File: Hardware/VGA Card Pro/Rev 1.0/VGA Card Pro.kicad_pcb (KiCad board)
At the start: 2 copper layers, 100 x 57.6 mm, 34 parts, among them J1 6502 Card Edge, J2 INT Select, J3 DE15_Receptacle_HighDensity_M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, J4 Conn_02x08_Odd_Even, Q1 BSS138, U1 Raspberry Pi Pico, U2 74LVC245, U3 74HCT245, U4 74LVC1G04, U5 74LVC245, U6 74HC138, U7 74HC138

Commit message: VGA Card layout
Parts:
- added C3: 100nF, Capacitor_SMD:C_0805_2012Metric, F.Cu at (148.0, 107.9)
- added C4: 100nF, Capacitor_SMD:C_0805_2012Metric, F.Cu at (178.2, 103.5)
- added C5: 100nF, Capacitor_SMD:C_0805_2012Metric, F.Cu at (118.8, 75.0)
- added C6: 100nF, Capacitor_SMD:C_0805_2012Metric, F.Cu at (168.4, 107.9)
- added C7: 100nF, Capacitor_SMD:C_0805_2012Metric, F.Cu at (115.3, 106.8)
- J3: value DE15_Receptacle_HighDensity_MountingHoles -> VGA
- moved R9 60.5 mm to (177.7, 95.6), turned to 0 degrees
- moved R10 56.5 mm to (177.7, 91.8), turned to 0 degrees
- moved R11 56.4 mm to (177.7, 99.5), turned to 0 degrees
- moved JP4 51.8 mm to (127.7, 118.4), turned to -90 degrees
- moved R5 51.6 mm to (171.9, 85.0), turned to 0 degrees
- moved JP3 51.4 mm to (124.8, 118.4)
- moved R6 49.8 mm to (171.9, 91.8), turned to 0 degrees
- moved R12 48.6 mm to (177.7, 81.1), turned to 0 degrees
- moved R7 48.0 mm to (171.9, 95.6), turned to 0 degrees
- moved R8 46.6 mm to (171.9, 99.5), turned to 0 degrees
- moved C1 46.2 mm to (127.7, 106.8), turned to 180 degrees
- moved R3 46.2 mm to (171.9, 77.2), turned to 0 degrees
- moved U2 44.4 mm to (162.9, 110.0), turned to 90 degrees
- moved R4 42.8 mm to (171.9, 81.1), turned to 0 degrees
- moved U4 42.1 mm to (174.2, 103.5), turned to 0 degrees
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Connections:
- C2 pad 1: VCC -> 3V3
- U4 pad 1: (no net) -> unconnected-(U4-NC-Pad1)
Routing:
- net CSB: track 22.4 -> 50.8 mm, vias 1 -> 2
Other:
- board text added: "IRQB"
- board text added: "JLCJLCJLCJLC"
- board text added: "NMIB"

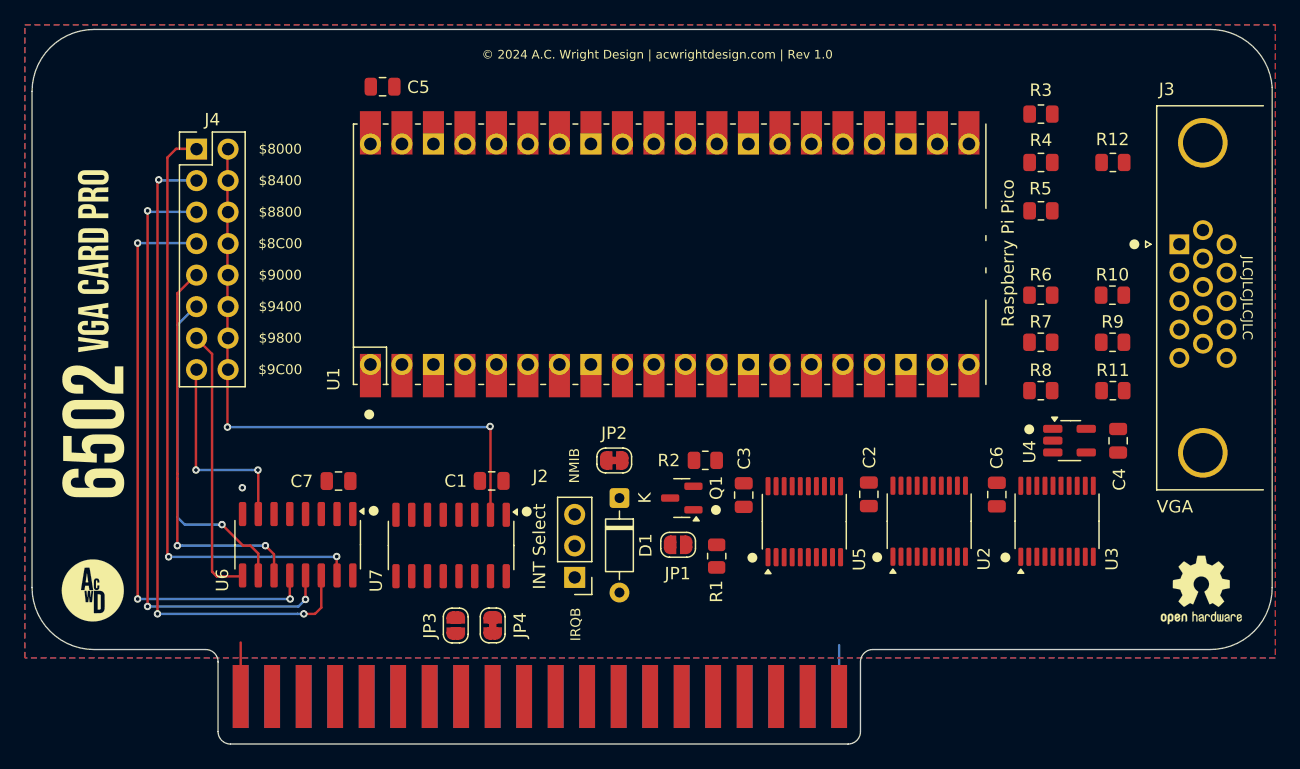
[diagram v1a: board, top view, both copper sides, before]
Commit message: Switch to 74LVC4245s
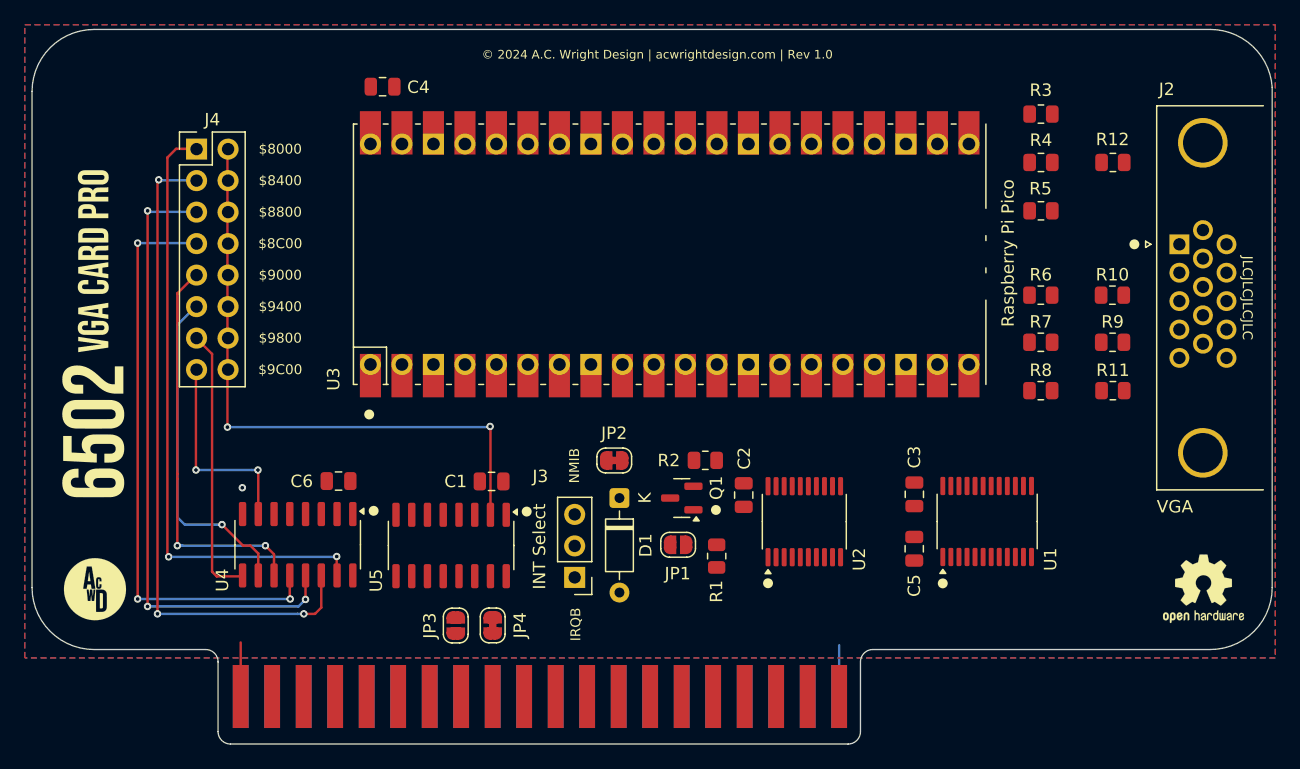
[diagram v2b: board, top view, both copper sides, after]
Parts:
- removed the C1 at (127.7, 106.8)
- removed the U2 at (162.9, 110.0)
- removed the U3 at (173.2, 110.0)
- removed the U4 at (174.2, 103.5)
- added U1: SN74LVC4245APWR, Package_SO:TSSOP-24_4.4x7.8mm_P0.65mm, F.Cu at (167.6, 110.0)
- U5: renamed from U7; value 74HC138 -> 74LVC138
- moved C1 30.4 mm to (127.6, 106.8), turned to 180 degrees
- moved C3 17.0 mm to (161.7, 107.9)
- moved C5 7.97 mm to (161.7, 112.2), turned to 90 degrees
- moved G*** 0.20 mm to (95.7, 115.5)
- moved REF** 0.20 mm to (185.0, 115.5)
- renumbered C2 to C1, C3 to C2, C4 to C3, C5 to C4, C6 to C5, C7 to C6, J3 to J2, J2 to J3, U5 to U2, U1 to U3, U6 to U4
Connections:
- J1 pad A3: unconnected-(J1-PadA3) -> A3
- U2 pad 13: unconnected-(U5-B5-Pad13) -> CSB_3V3
- U2 pad 14: unconnected-(U5-B4-Pad14) -> RESB_3V3
- U2 pad 15: RESB_3V3 -> A3_3V3
- U2 pad 5: RESB -> A3
- U2 pad 6: GND -> RESB
- U2 pad 7: GND -> CSB
- U3 pad 16: CSRB_3V3 -> A2_3V3
- U3 pad 17: CSWB_3V3 -> INTB_3V3
- U3 pad 29: A2_3V3 -> A3_3V3
- U3 pad 31: INTB_3V3 -> RESB_3V3
- U3 pad 32: RESB_3V3 -> CSB_3V3
- U3 pad 34: OEB_3V3 -> RWB_3V3
- U5 pad 14: CSRB_3V3 -> RWBB_3V3
- U5 pad 15: CSWB_3V3 -> RWB_3V3

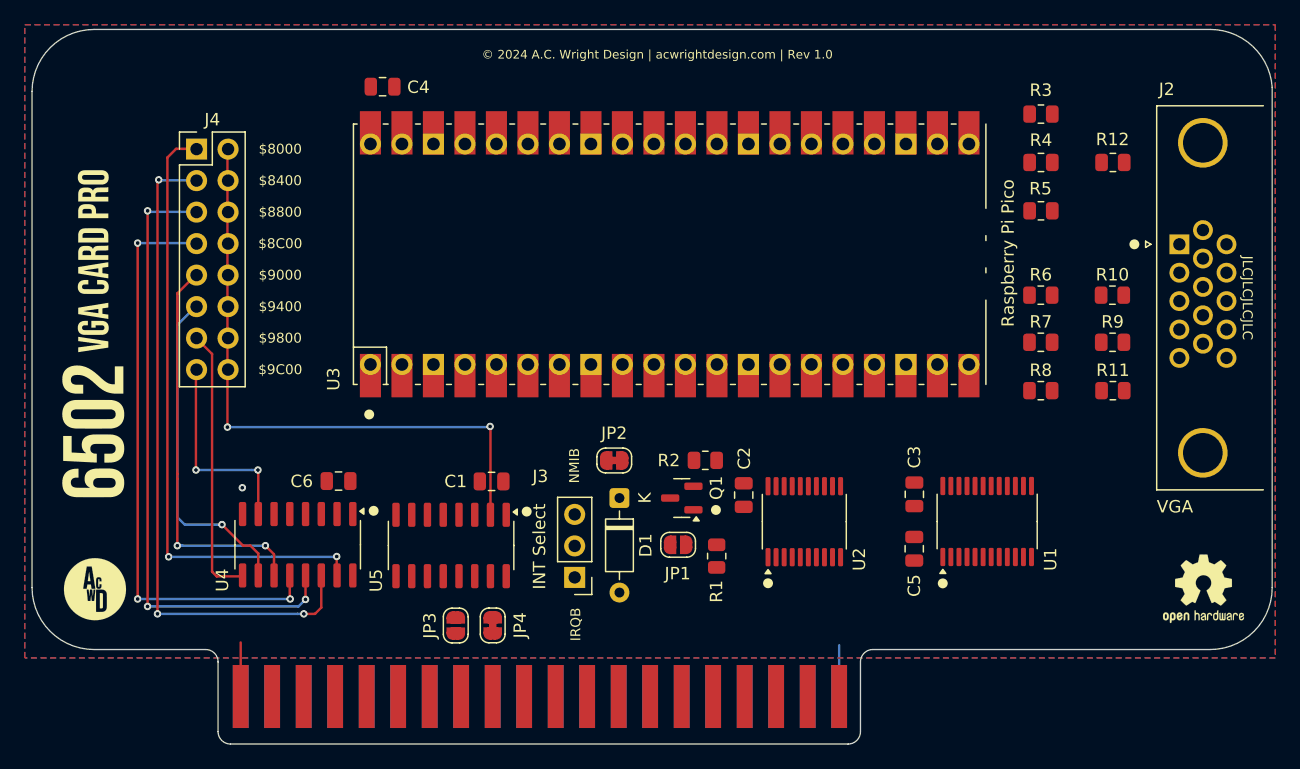
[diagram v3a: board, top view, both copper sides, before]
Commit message: Add VGA Card Pro PCB
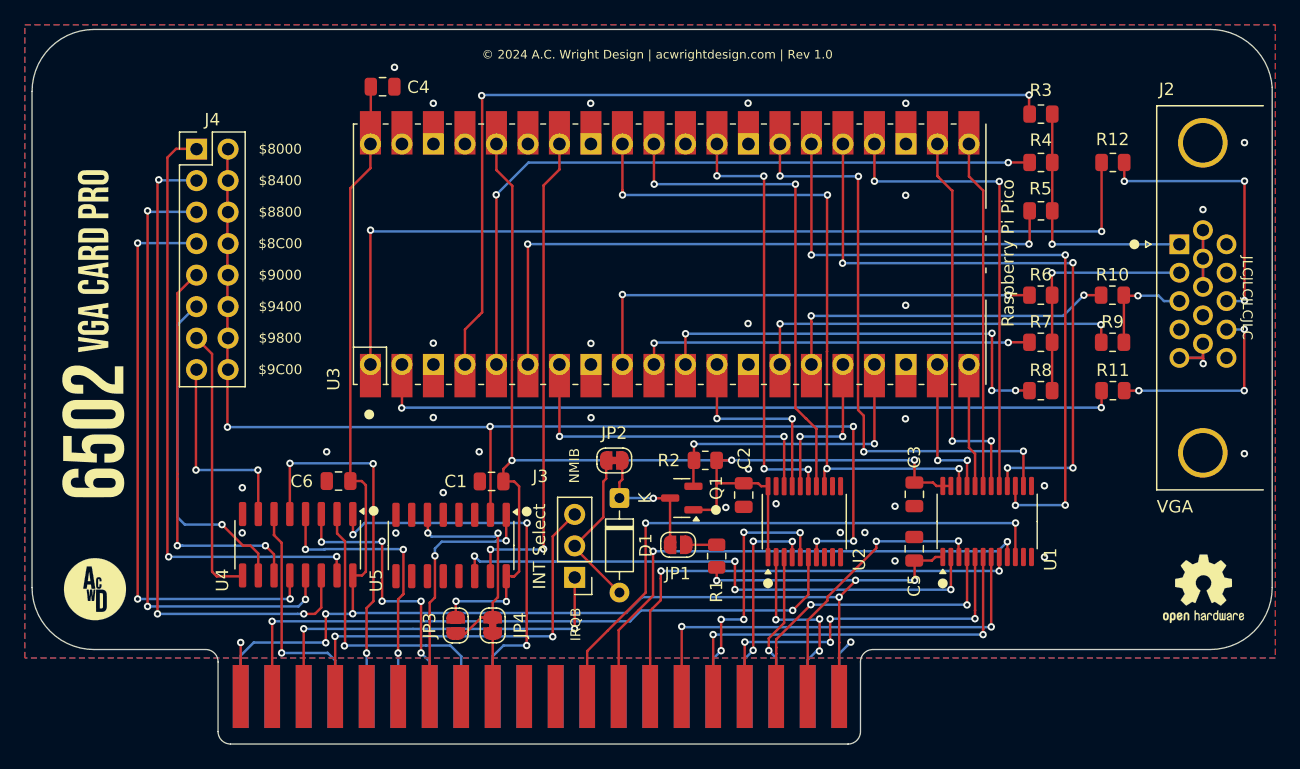
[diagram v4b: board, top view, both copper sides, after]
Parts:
- turned JP3 to -90 degrees
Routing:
- net VCC: track 0.06 -> 131.1 mm, vias 0 -> 7
- net 3V3: track 0.00 -> 99.3 mm, vias 0 -> 5
- net HSYNC: track 0.00 -> 75.4 mm, vias 0 -> 2
- net R0: track 0.00 -> 68.0 mm, vias 0 -> 2
- net VSYNC: track 0.00 -> 61.3 mm, vias 0 -> 2
- net R1: track 0.00 -> 57.8 mm, vias 0 -> 2
- net CSB_3V3: track 0.00 -> 56.3 mm, vias 0 -> 4
- net D6_3V3: track 0.00 -> 55.2 mm, vias 0 -> 4
- net RESB: track 0.00 -> 53.2 mm, vias 0 -> 2
- net R2: track 0.00 -> 52.9 mm, vias 0 -> 2
- net D5_3V3: track 0.00 -> 51.5 mm, vias 0 -> 4
- net D7: track 0.00 -> 48.5 mm, vias 0 -> 2
- net D7_3V3: track 0.00 -> 47.0 mm, vias 0 -> 4
- net RWBB_3V3: track 0.00 -> 45.2 mm, vias 0 -> 4
- net D6: track 0.00 -> 43.0 mm, vias 0 -> 2
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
